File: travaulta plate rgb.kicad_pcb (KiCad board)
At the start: 4 copper layers, 209.7 x 76.4 mm, 59 parts

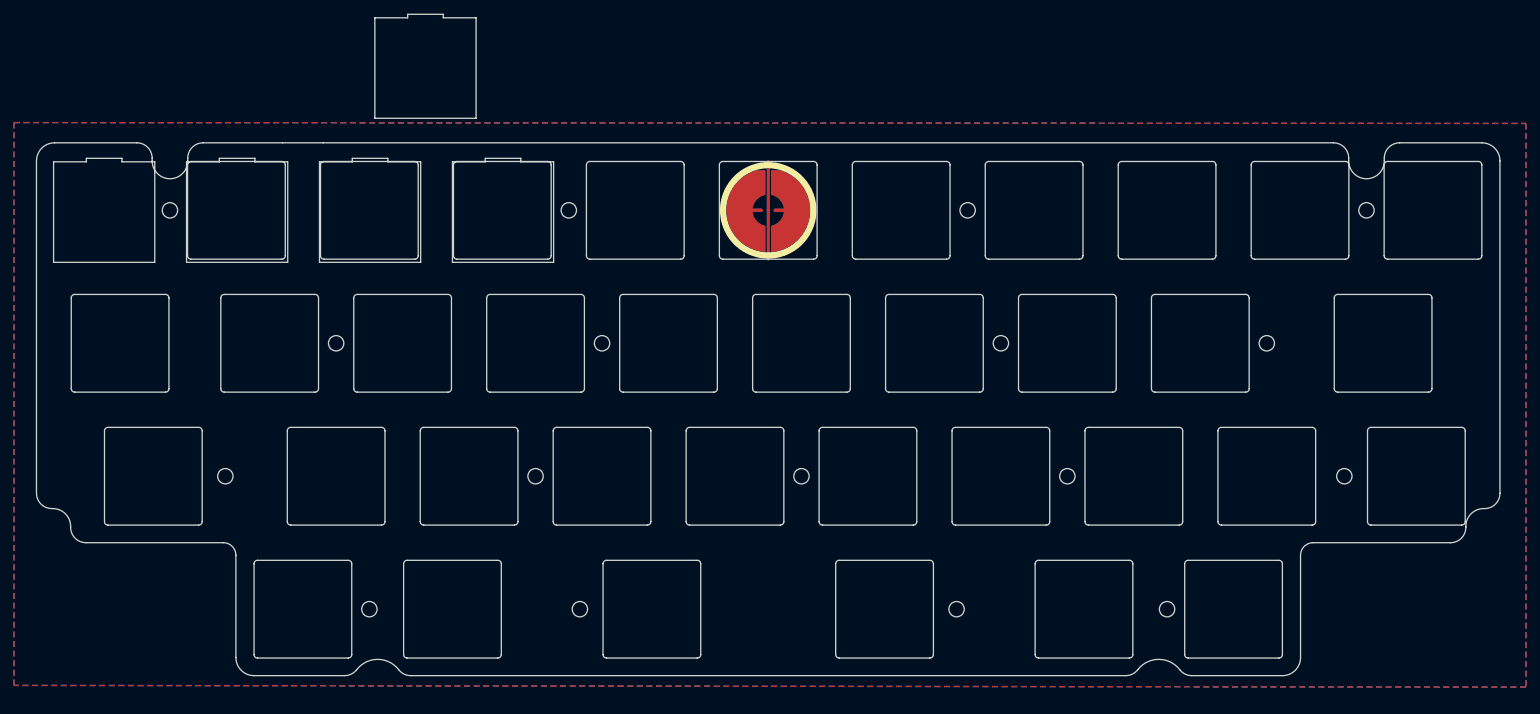
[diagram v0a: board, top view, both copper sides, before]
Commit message: plate cutouts
needs plate edge cut
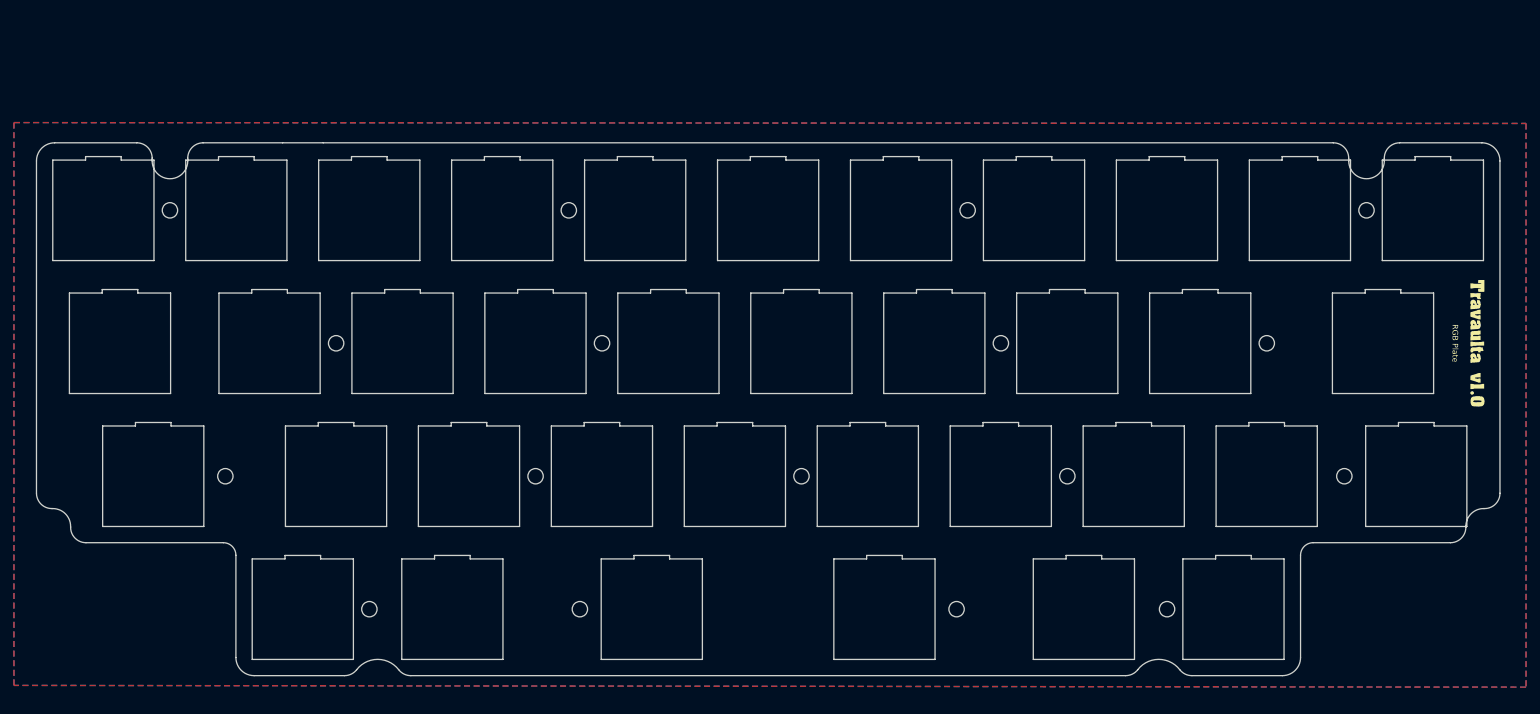
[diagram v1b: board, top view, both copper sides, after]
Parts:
- removed ? (x16): , 
- removed REF** (x41): Value, cipulot_parts:plate_cut_ecs_pad_NIZ
- removed REF**: Value, cipulot_parts:ecs_pad_1U_no_ring_1u_edge_cut
- added G***: LOGO, LOGO, F.Cu at (250.8, 76.2)
- added H1: MountingHole, cipulot_parts:HOLE_M2, F.Cu at (63.5, 57.1)
- added H10: MountingHole, cipulot_parts:HOLE_M2, F.Cu at (115.9, 95.2)
- added H11: MountingHole, cipulot_parts:HOLE_M2, F.Cu at (154.0, 95.2)
- added H12: MountingHole, cipulot_parts:HOLE_M2, F.Cu at (192.1, 95.2)
- added H13: MountingHole, cipulot_parts:HOLE_M2, F.Cu at (231.8, 95.2)
- added H14: MountingHole, cipulot_parts:HOLE_M2, F.Cu at (92.1, 114.3)
- added H15: MountingHole, cipulot_parts:HOLE_M2, F.Cu at (122.2, 114.3)
- added H16: MountingHole, cipulot_parts:HOLE_M2, F.Cu at (176.2, 114.3)
- added H17: MountingHole, cipulot_parts:HOLE_M2, F.Cu at (206.4, 114.3)
- added H2: MountingHole, cipulot_parts:HOLE_M2, F.Cu at (120.7, 57.1)
- added H3: MountingHole, cipulot_parts:HOLE_M2, F.Cu at (177.8, 57.1)
- added H4: MountingHole, cipulot_parts:HOLE_M2, F.Cu at (234.9, 57.1)
- added H6: MountingHole, cipulot_parts:HOLE_M2, F.Cu at (125.4, 76.2)
- added H7: MountingHole, cipulot_parts:HOLE_M2, F.Cu at (182.6, 76.2)
- added H8: MountingHole, cipulot_parts:HOLE_M2, F.Cu at (220.7, 76.2)
- added H9: MountingHole, cipulot_parts:HOLE_M2, F.Cu at (71.4, 95.2)
- added RGB topre: RGB realforce R2, lib:RGB realforce R2, F.Cu at (61.1, 95.2)
- added RGB topre: RGB realforce R2, lib:RGB realforce R2, F.Cu at (144.5, 95.2)
- added RGB topre: RGB realforce R2, lib:RGB realforce R2, F.Cu at (220.7, 95.2)
- added RGB topre: RGB realforce R2, lib:RGB realforce R2, F.Cu at (82.5, 114.3)
- added RGB topre: RGB realforce R2, lib:RGB realforce R2, F.Cu at (130.2, 57.1)
- added RGB topre: RGB realforce R2, lib:RGB realforce R2, F.Cu at (134.9, 76.2)
- added RGB topre: RGB realforce R2, lib:RGB realforce R2, F.Cu at (104.0, 114.3)
- added RGB topre: RGB realforce R2, lib:RGB realforce R2, F.Cu at (106.4, 95.2)
- added RGB topre: RGB realforce R2, lib:RGB realforce R2, F.Cu at (56.4, 76.2)
- added RGB topre: RGB realforce R2, lib:RGB realforce R2, F.Cu at (92.1, 57.1)
- added RGB topre: RGB realforce R2, lib:RGB realforce R2, F.Cu at (244.5, 57.1)
- added RGB topre: RGB realforce R2, lib:RGB realforce R2, F.Cu at (187.3, 57.1)
- added RGB topre: RGB realforce R2, lib:RGB realforce R2, F.Cu at (237.3, 76.2)
- added RGB topre: RGB realforce R2, lib:RGB realforce R2, F.Cu at (182.6, 95.2)
- added RGB topre: RGB realforce R2, lib:RGB realforce R2, F.Cu at (225.4, 57.1)
- added RGB topre: RGB realforce R2, lib:RGB realforce R2, F.Cu at (87.3, 95.2)
- added RGB topre: RGB realforce R2, lib:RGB realforce R2, F.Cu at (165.9, 114.3)
- added RGB topre: RGB realforce R2, lib:RGB realforce R2, F.Cu at (149.2, 57.1)
- added RGB topre: RGB realforce R2, lib:RGB realforce R2, F.Cu at (242.1, 95.2)
- added RGB topre: RGB realforce R2, lib:RGB realforce R2, F.Cu at (111.1, 57.1)
- added RGB topre: RGB realforce R2, lib:RGB realforce R2, F.Cu at (154.0, 76.2)
- added RGB topre: RGB realforce R2, lib:RGB realforce R2, F.Cu at (132.6, 114.3)
- added RGB topre: RGB realforce R2, lib:RGB realforce R2, F.Cu at (194.5, 114.3)
- added RGB topre: RGB realforce R2, lib:RGB realforce R2, F.Cu at (54.0, 57.1)
- added RGB topre: RGB realforce R2, lib:RGB realforce R2, F.Cu at (125.4, 95.2)
- added RGB topre: RGB realforce R2, lib:RGB realforce R2, F.Cu at (215.9, 114.3)
- added RGB topre: RGB realforce R2, lib:RGB realforce R2, F.Cu at (73.0, 57.1)
- added RGB topre: RGB realforce R2, lib:RGB realforce R2, F.Cu at (201.6, 95.2)
- added RGB topre: RGB realforce R2, lib:RGB realforce R2, F.Cu at (115.9, 76.2)
- added RGB topre: RGB realforce R2, lib:RGB realforce R2, F.Cu at (173.0, 76.2)
- added RGB topre: RGB realforce R2, lib:RGB realforce R2, F.Cu at (163.5, 95.2)
- added RGB topre: RGB realforce R2, lib:RGB realforce R2, F.Cu at (96.8, 76.2)
- added RGB topre: RGB realforce R2, lib:RGB realforce R2, F.Cu at (192.1, 76.2)
- added RGB topre: RGB realforce R2, lib:RGB realforce R2, F.Cu at (168.3, 57.1)
- added RGB topre: RGB realforce R2, lib:RGB realforce R2, F.Cu at (211.1, 76.2)
- added RGB topre: RGB realforce R2, lib:RGB realforce R2, F.Cu at (77.8, 76.2)
- added RGB topre: RGB realforce R2, lib:RGB realforce R2, F.Cu at (206.4, 57.1)
- moved H5 34.3 mm to (87.3, 76.2)
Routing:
- removed copper zone on In1.Cu, net GND
- removed copper zone on In2.Cu, net GND
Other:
- copper layers 4 -> 2
- board text added: "RGB Plate"
- board text removed: "SW1"

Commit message: first draft plates complete
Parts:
- turned RGB topre to 180 degrees (x4)
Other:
- board size 209.7 x 76.4 mm -> 210.7 x 77.4 mm

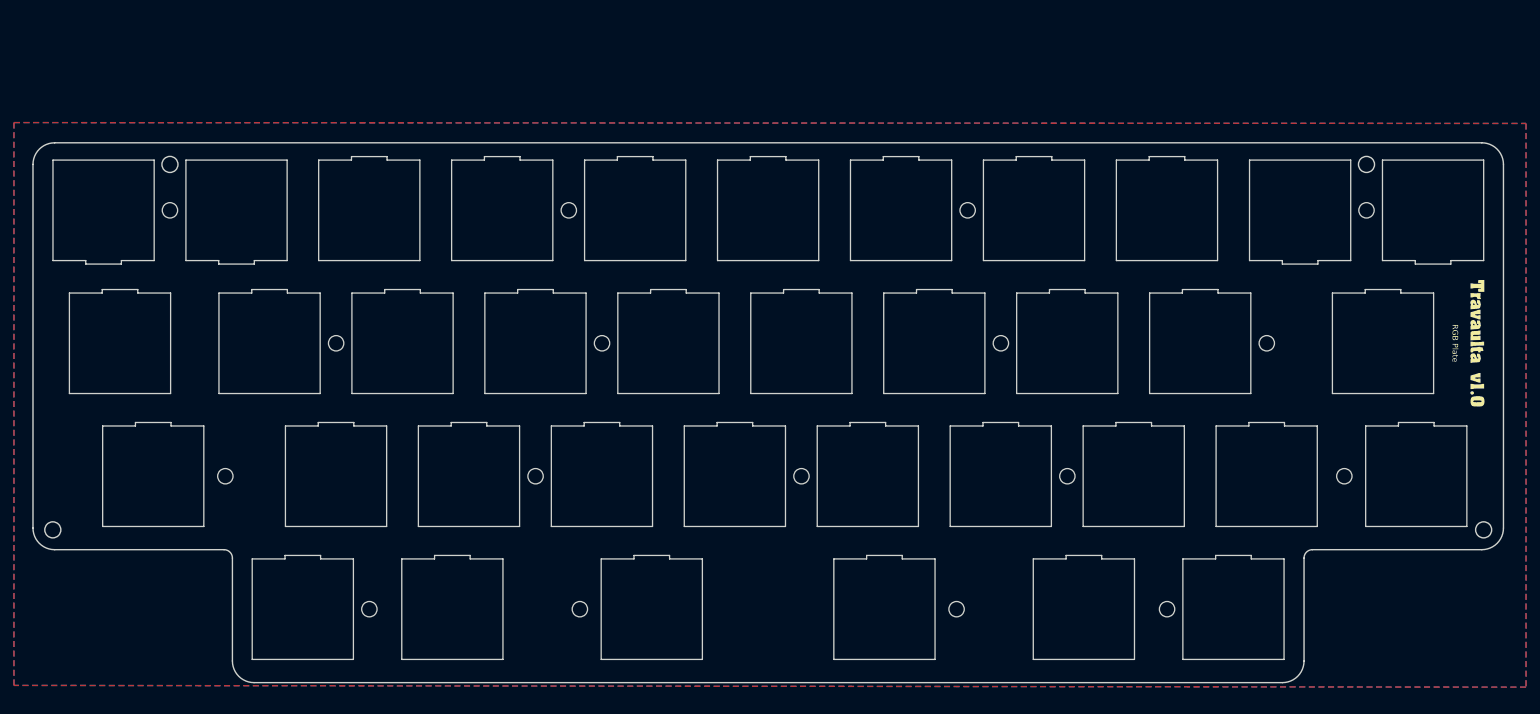
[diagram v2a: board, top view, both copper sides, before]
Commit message: edited preliminary firmware, small routing cleanups
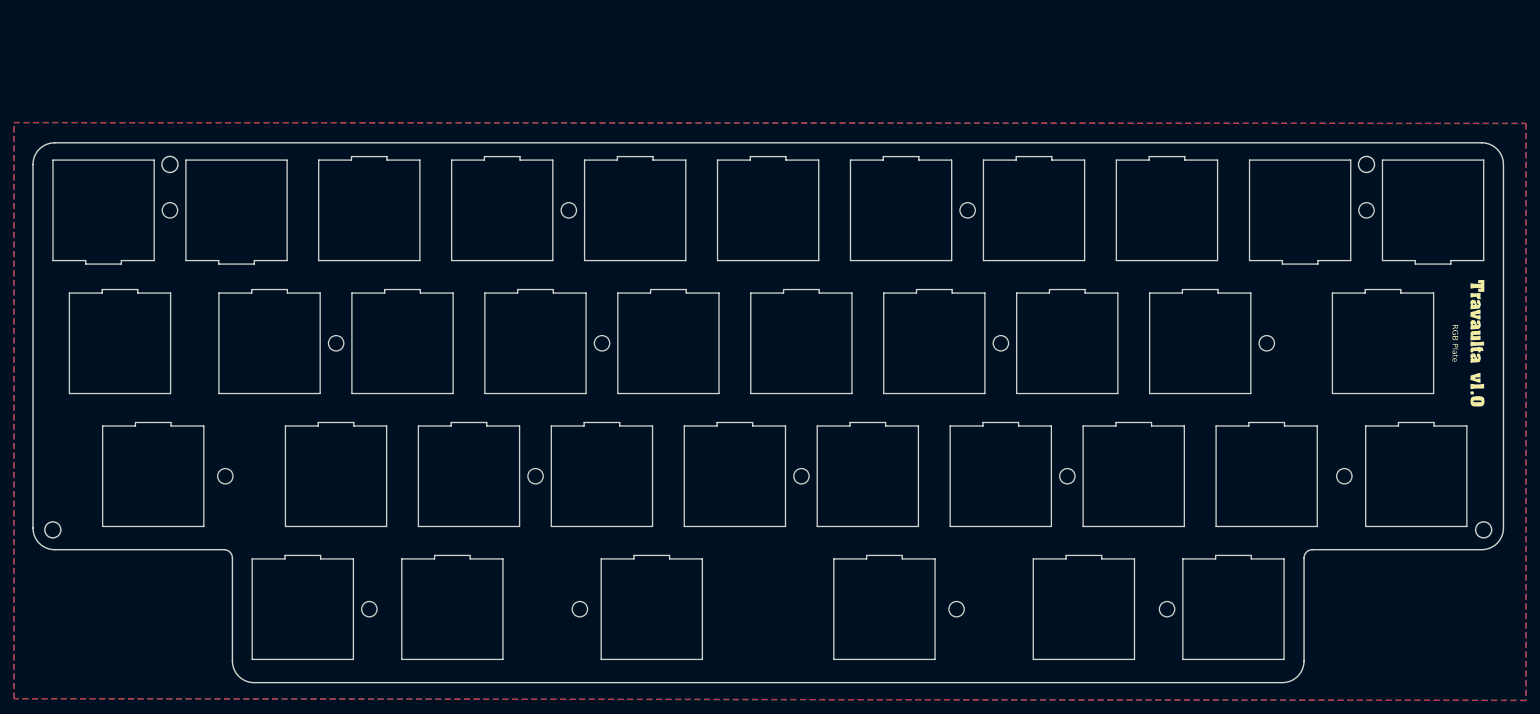
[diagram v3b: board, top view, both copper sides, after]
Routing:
- added copper zone on B.Cu, net (none)
- added copper zone on F.Cu, net (none)
- removed copper zone on B.Cu, net GND
- removed copper zone on F.Cu, net GND

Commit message: fresh gerbers
deleted old plate gerbers, need new export
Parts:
- moved H16 0.79 mm to (175.4, 114.3)
- moved H15 0.79 mm to (123.0, 114.3)
- moved H9 0.79 mm to (70.6, 95.2)
- moved H13 0.79 mm to (232.6, 95.2)
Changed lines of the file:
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@@
   )
   (footprint "cipulot_parts:HOLE_M2" (layer "F.Cu")
-    (at 71.4375 95.25)
+    (at 70.64375 95.25)
     (property "Sheetfile" "mounting holes.kicad_sch")
     (property "Sheetname" "mounting holes")
@@
   )
   (footprint "cipulot_parts:HOLE_M2" (layer "F.Cu")
-    (at 231.775 95.25)
+    (at 232.56875 95.25)
     (property "Sheetfile" "mounting holes.kicad_sch")
     (property "Sheetname" "mounting holes")
@@
   )
   (footprint "cipulot_parts:HOLE_M2" (layer "F.Cu")
-    (at 122.2375 114.3)
+    (at 123.03125 114.3)
     (property "Sheetfile" "mounting holes.kicad_sch")
     (property "Sheetname" "mounting holes")
@@
   )
   (footprint "cipulot_parts:HOLE_M2" (layer "F.Cu")
-    (at 176.2125 114.3)
-    (property "Sheetfile" "mounting holes.kicad_sch")
-    (property "Sheetname" "mounting holes")
+    (at 175.41875 114.3)
+    (property "Sheetfile" "mounting holes.kicad_sch")
+    (property "Sheetname" "mounting holes")

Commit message: pcb clean up, fresh gerbers
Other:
- board text added: "JLCJLCJLCJLC"
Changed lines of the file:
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@@
   (gr_circle (center 63.5 50.574999) (end 64.65 50.574999)
     (stroke (width 0.2) (type solid)) (fill none) (layer "Edge.Cuts"))
+  (gr_text "JLCJLCJLCJLC" (at 249.2375 76.2 -90) (layer "B.SilkS")
+    (effects (font (size 1 1) (thickness 0.15)))
+  )
   (gr_text "RGB Plate" (at 247.65 76.2 270) (layer "F.SilkS")
     (effects (font (size 0.8 0.8) (thickness 0.15)))
